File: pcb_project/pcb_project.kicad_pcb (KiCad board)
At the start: 6 copper layers, 246 parts, among them IC1 TPS54325PWPR, IC2 TPS54294PWPR, IC3 IS61WV204816BLL-10TLI, IC4 IS61WV204816BLL-10TLI, J1 USB1130-15-A_REVA, J10 M20-9990246, J11 M20-9990246, J12 M20-9990246, J13 Conn_01x10_Pin, J2 FTSH-107-01-F-DV-K, J3 Conn_ST_STDC14, J4 DE15_Socket_HighDensity_Mount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, J5 USB_B_Micro, J6 MEM2052-00-195-00-A, J8 M20-9990246, J9 M20-9990246, Q1 BC857BS, Q2 BC847BPN, SW2 SW_SPDT, SW3 SW_SPST, SW4 SW_SPST, U1 XC7A100T-FTG256, U10 TPD1E1B04DPYT, U11 TPD1E1B04DPYT, U12 TPD1E1B04DPYT, U13 TPD1E1B04DPYT, U2 STM32U595VJTx, U3 TPS2041B, U4 D3V3XA4B10LP, U5 TPD1E1B04DPYT, U6 TPD1E1B04DPYT, U7 MAX7221xWG, U8 COM-11405, U9 MT25QL128ABA1ESE-0SIT, Y1 48MHz, Y2 XLH736025.175000I

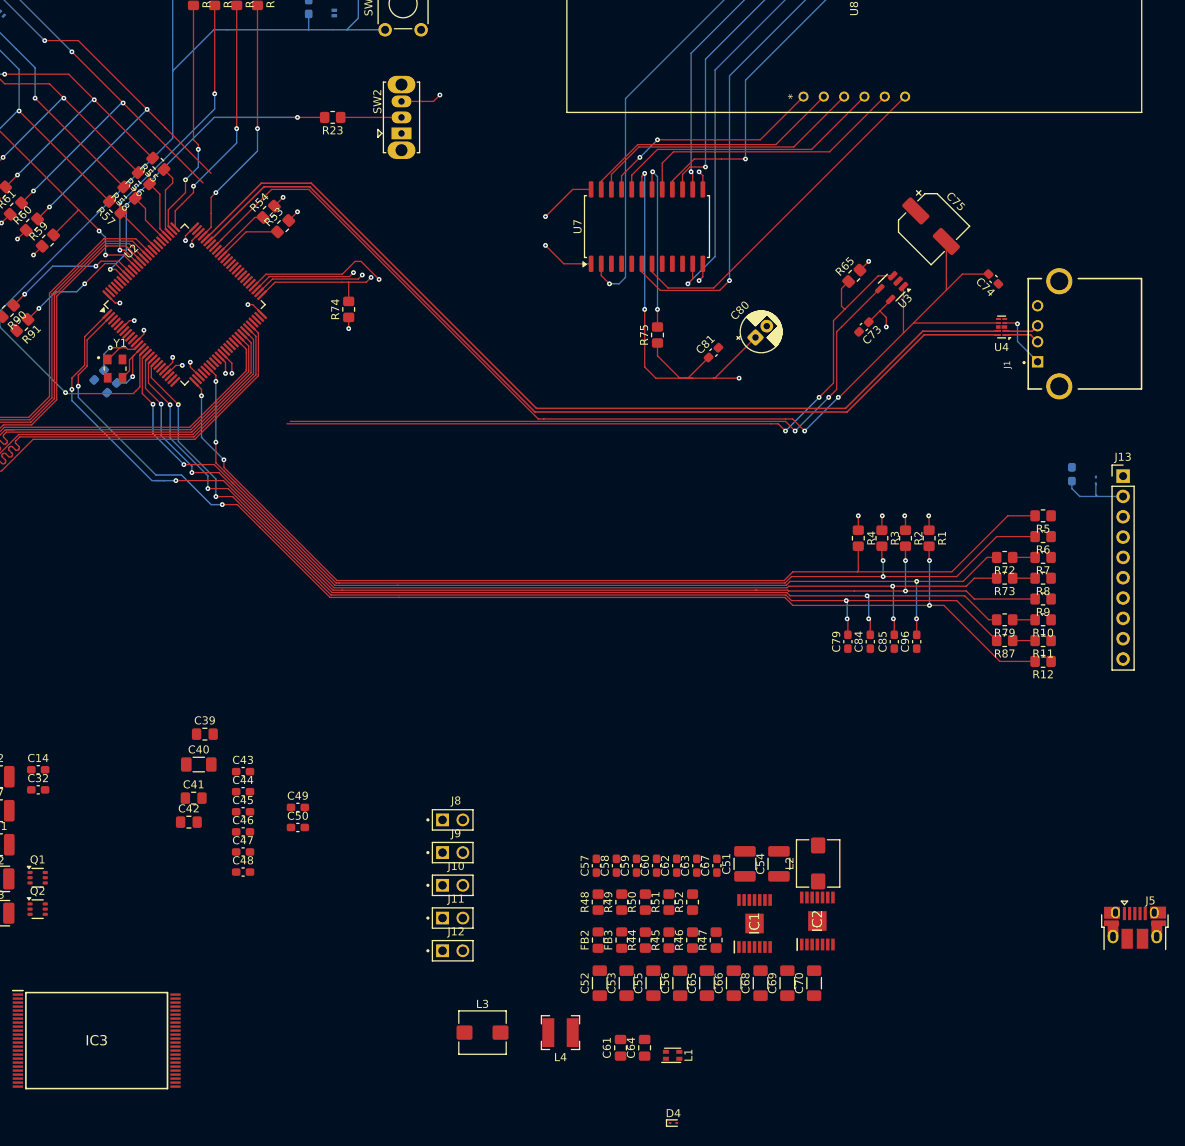
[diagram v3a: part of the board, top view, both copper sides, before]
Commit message: Power supply layout
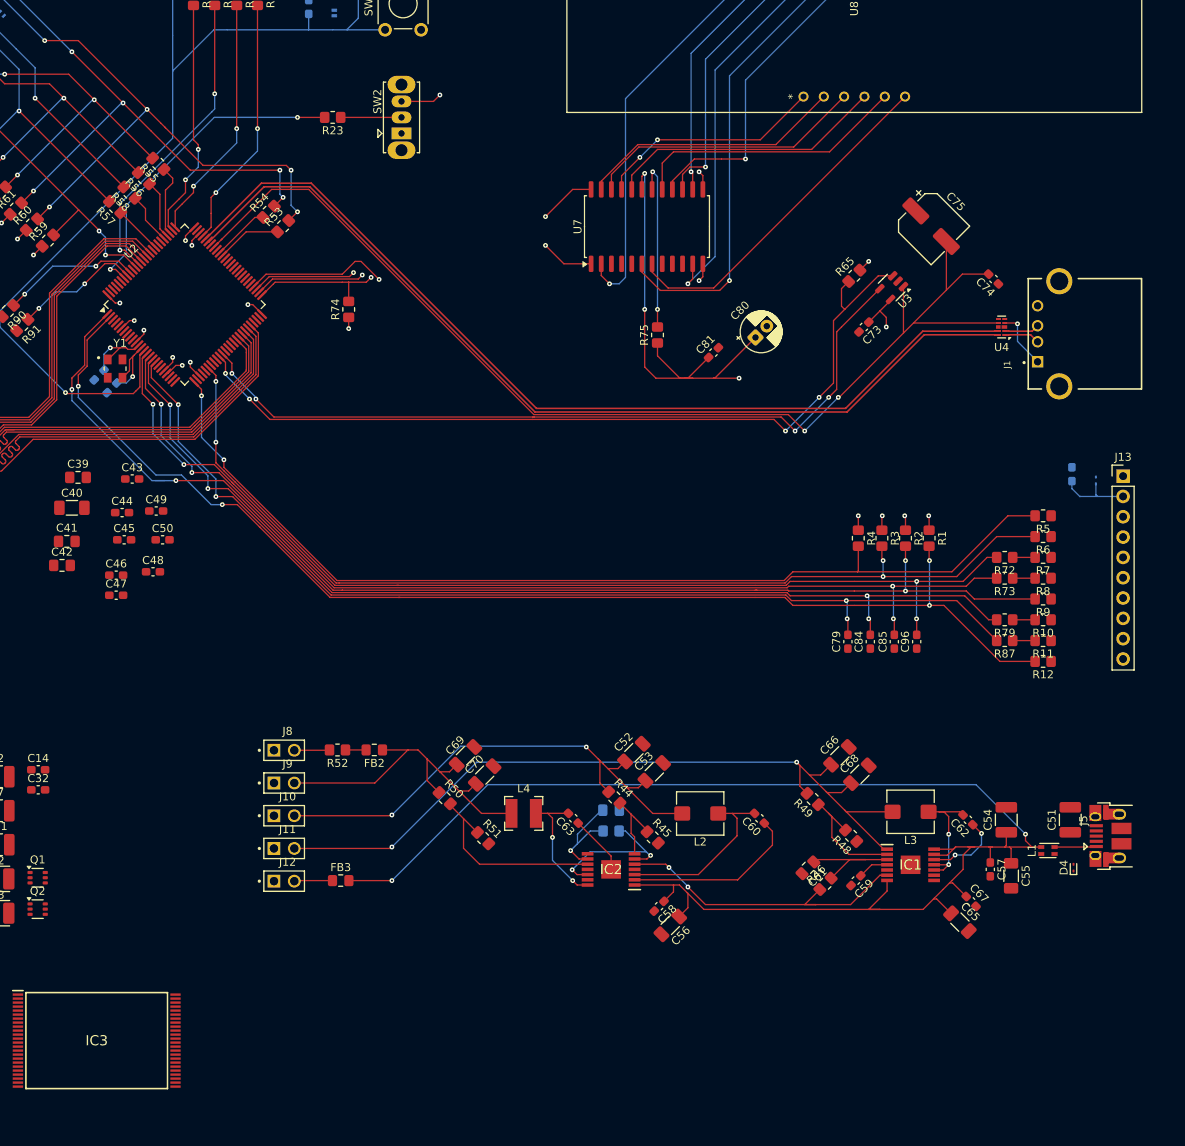
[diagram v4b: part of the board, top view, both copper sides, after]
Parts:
- C64, R47: moved to B.Cu
- moved L3 60.2 mm to (233.2, 133.4), turned to 180 degrees
- moved D4 59.3 mm to (253.6, 140.4), turned to 90 degrees
- moved L1 53.4 mm to (250.4, 138.2), turned to -90 degrees
- moved C69 49.3 mm to (177.6, 126.4), turned to 45 degrees
- moved C57 49.2 mm to (243.2, 140.6), turned to -90 degrees
- moved C70 48.7 mm to (180.0, 128.8), turned to 45 degrees
- moved R52 48.3 mm to (161.6, 125.7), turned to 180 degrees
- moved C55 46.7 mm to (245.8, 141.4), turned to -90 degrees
- moved C49 41.1 mm to (138.9, 95.8)
- moved C51 41.0 mm to (253.2, 134.4)
- moved C50 39.7 mm to (139.7, 99.4)
- moved C48 39.2 mm to (138.5, 103.4)
- moved C43 39.1 mm to (135.9, 91.8)
- moved C44 38.0 mm to (134.7, 96.0)
- moved C45 37.1 mm to (134.9, 99.4)
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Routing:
- net Net-(IC1-EN): track 0.00 -> 182.8 mm, vias 0 -> 2
- net Net-(IC1-VO): track 0.00 -> 100.1 mm, vias 0 -> 2
- net Net-(C52-Pad1): track 0.00 -> 65.8 mm, vias 0 -> 2
- net Net-(C69-Pad1): track 0.00 -> 45.0 mm
- net Net-(IC1-PG): track 0.00 -> 39.3 mm, vias 0 -> 2
- net Net-(IC2-VFB2): track 0.00 -> 25.0 mm
- net Net-(IC2-SW1): track 0.00 -> 22.4 mm
- net Net-(IC2-VBST1): track 0.00 -> 22.2 mm
- net Net-(IC2-EN2): track 0.00 -> 19.8 mm, vias 0 -> 2
- net Net-(IC2-SW2): track 0.00 -> 15.9 mm, vias 0 -> 2
- net Net-(IC1-SW1): track 0.00 -> 15.9 mm, vias 0 -> 2
- net Net-(IC1-VFB): track 0.00 -> 15.6 mm
- net Net-(J6-DAT0): track 64.1 -> 79.4 mm, vias 5 -> 6
- net Net-(IC1-VREG5): track 0.00 -> 14.5 mm
- net Net-(IC2-VREG5): track 0.00 -> 13.2 mm, vias 0 -> 1
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
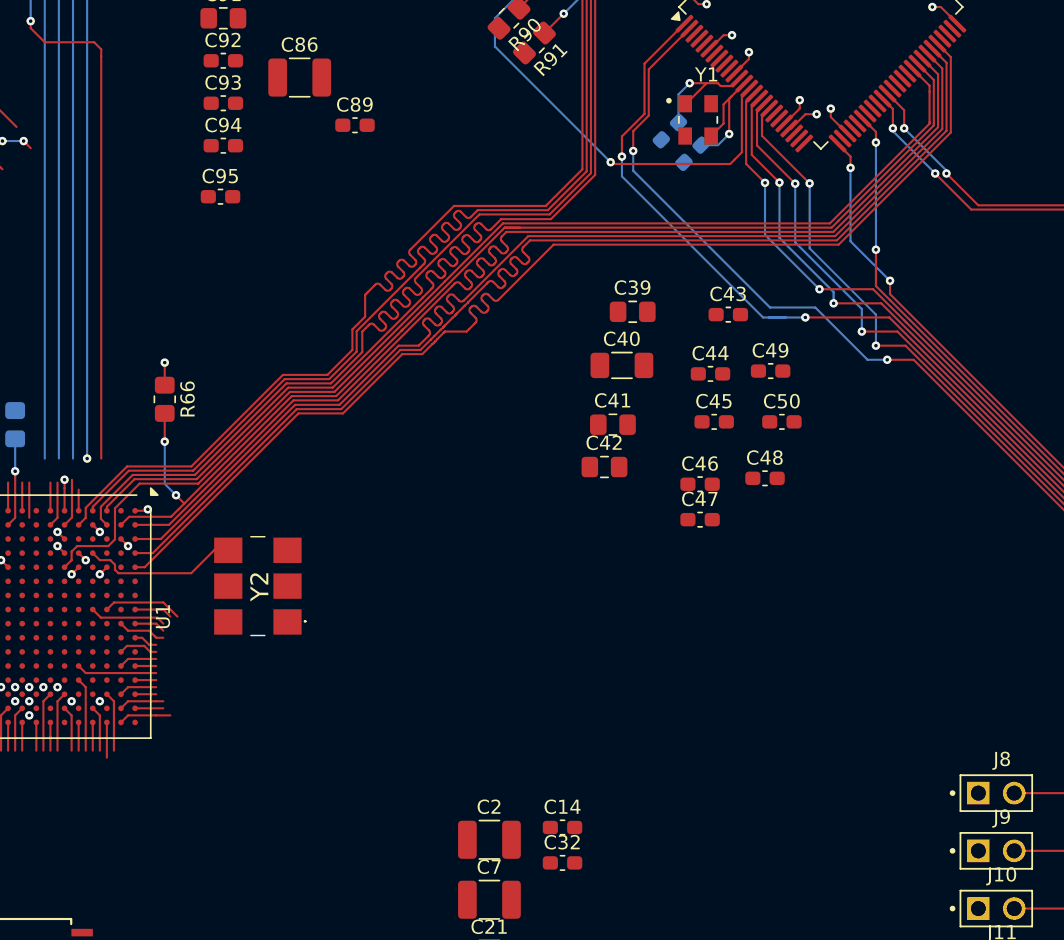
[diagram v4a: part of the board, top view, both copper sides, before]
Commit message: More length matching OSPI
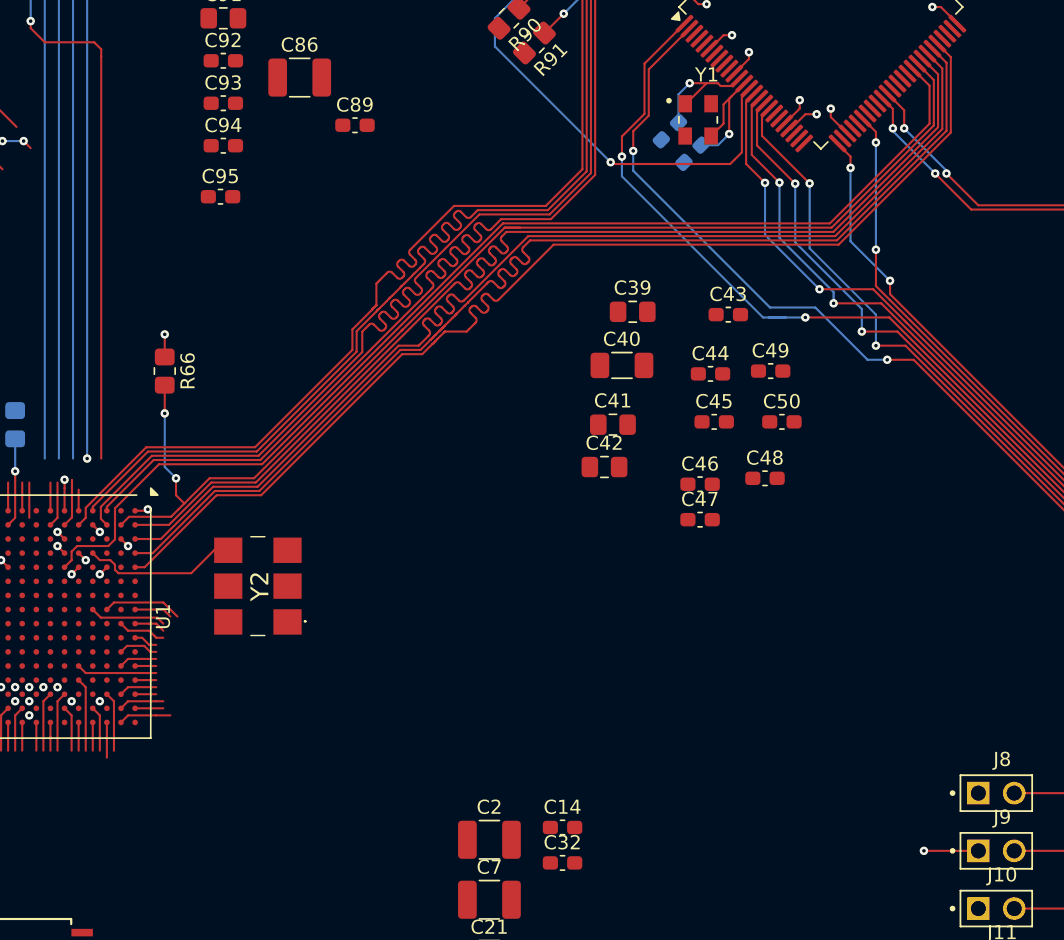
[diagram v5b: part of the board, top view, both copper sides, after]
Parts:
- moved R66 2.00 mm to (96.0, 95.8)
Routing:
- net +3V3: track 81.3 -> 85.2 mm, vias 28 -> 29
- net /FPGA/OSPI CS: track 82.4 -> 84.4 mm
- net /FPGA/OSPI 4: track 82.0 -> 80.4 mm

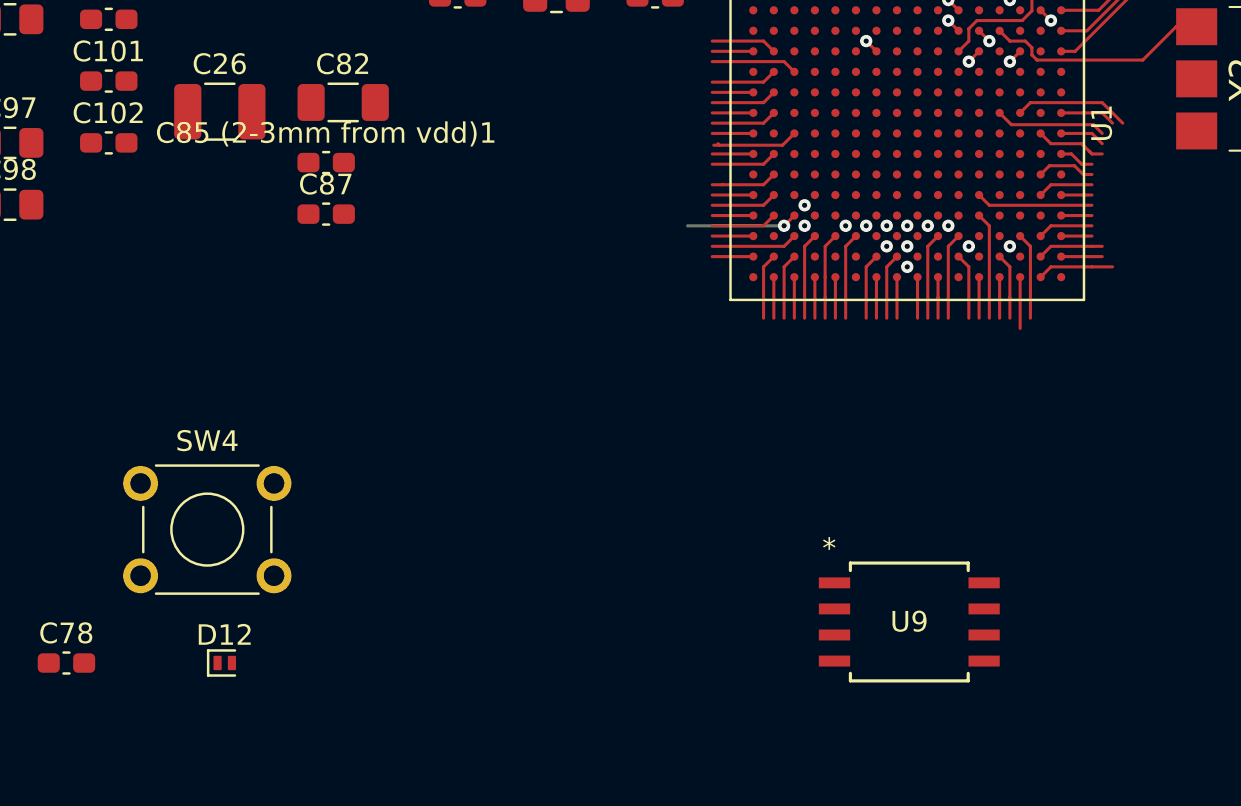
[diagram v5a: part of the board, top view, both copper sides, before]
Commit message: More fpga outwires
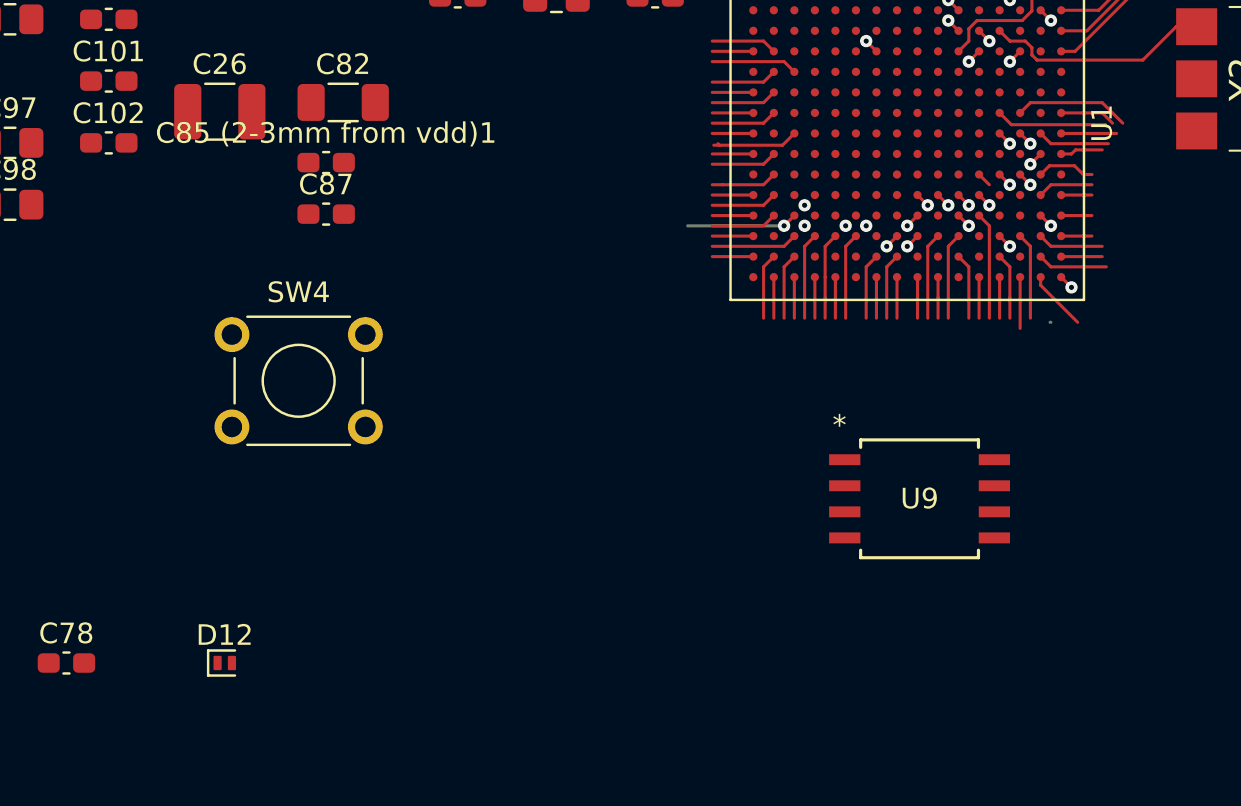
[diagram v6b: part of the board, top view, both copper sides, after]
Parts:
- moved SW4 8.51 mm to (53.5, 123.5)
- moved U9 6.02 mm to (87.0, 131.5)
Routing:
- net /FPGA/A_Bank14&15/WE: track 0.00 -> 9.17 mm, vias 0 -> 1
- net Net-(IC3-I/O8): track 0.00 -> 8.55 mm, vias 0 -> 1
- net Net-(IC3-I/O3): track 0.00 -> 8.26 mm, vias 0 -> 1
- net Net-(IC3-I/O4): track 0.00 -> 7.35 mm, vias 0 -> 1
- net Net-(IC3-A11): track 0.00 -> 6.13 mm, vias 0 -> 1
- net /FPGA/A_Bank14&15/LB: track 0.00 -> 5.80 mm, vias 0 -> 1
- net Net-(IC3-A1): track 0.00 -> 4.88 mm, vias 0 -> 1
- net Net-(IC3-A6): track 0.00 -> 4.85 mm, vias 0 -> 1
- net Net-(U1A-IO_L1N_T0_D01_DIN_14): track 0.00 -> 4.63 mm, vias 0 -> 1
- net /FPGA/A_Bank14&15/A20: track 0.00 -> 4.60 mm, vias 0 -> 1
- net Net-(IC3-I/O15): track 0.00 -> 4.60 mm, vias 0 -> 1
- net Net-(IC3-I/O0): track 5.71 -> 8.32 mm, vias 0 -> 1
- net +3V3: track 85.2 -> 86.6 mm, vias 29 -> 31
- net Net-(IC3-A19): track 3.71 -> 2.95 mm
- net Net-(IC3-I/O9): track 0.00 -> 0.71 mm, vias 0 -> 1
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
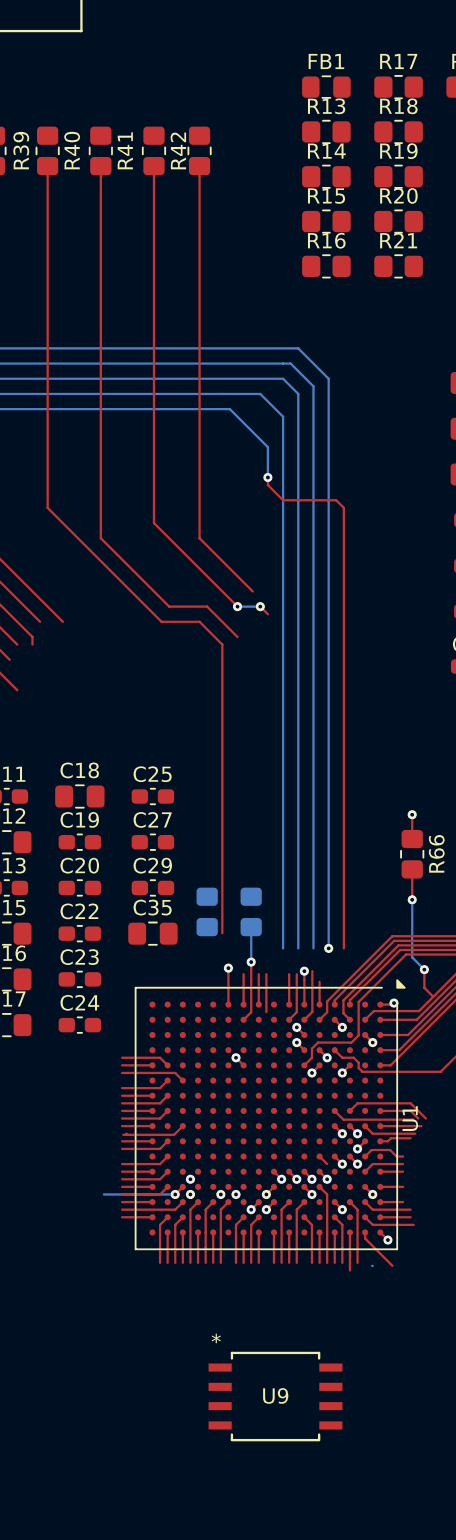
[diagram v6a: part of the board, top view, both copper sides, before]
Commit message: More FPGA ballout
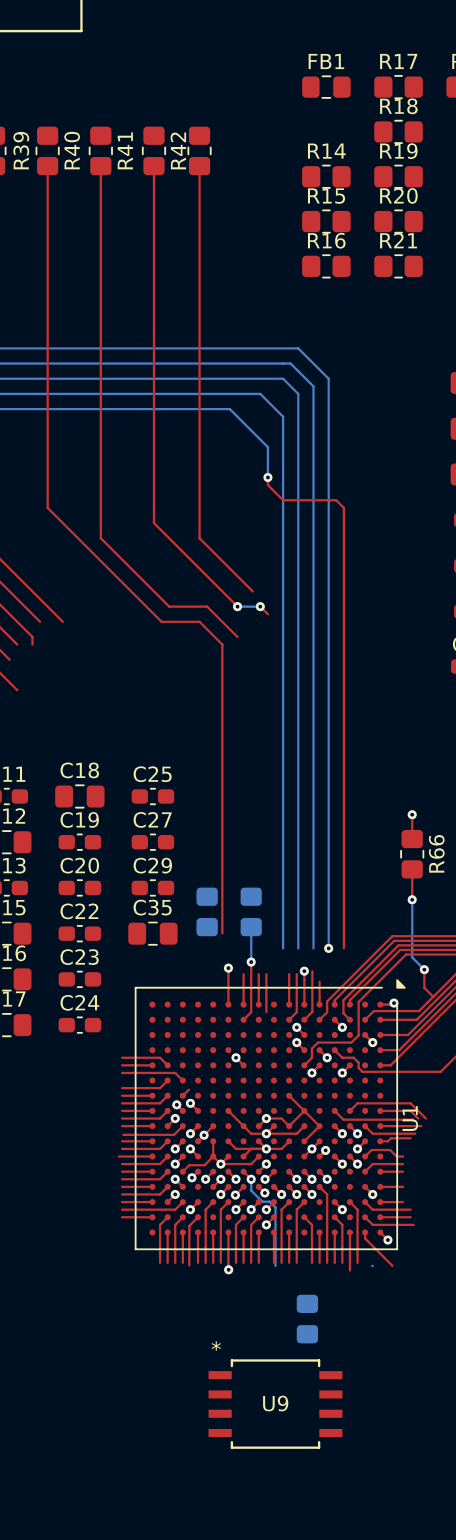
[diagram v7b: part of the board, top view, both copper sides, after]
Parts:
- R13: moved to B.Cu
- moved R13 78.2 mm to (89.1, 126.4), turned to -90 degrees
- moved U9 0.50 mm to (87.0, 132.0)
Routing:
- net GND: track 5.53 -> 26.7 mm, vias 4 -> 9
- net +3V3: track 86.6 -> 96.1 mm, vias 31 -> 37
- net Net-(IC4-LB#): track 0.00 -> 8.44 mm, vias 0 -> 1
- net Net-(U1A-IO_L6P_T0_FCS_B_14): track 0.00 -> 8.00 mm, vias 0 -> 1
- net +1V0: track 0.00 -> 7.95 mm, vias 0 -> 2
- net Net-(IC4-I/O15): track 0.00 -> 7.36 mm, vias 0 -> 1
- net Net-(IC3-I/O2): track 0.71 -> 8.06 mm, vias 0 -> 1
- net +1V8: track 0.00 -> 6.83 mm, vias 0 -> 1
- net Net-(IC4-UB#): track 0.00 -> 6.54 mm, vias 0 -> 1
- net Net-(IC4-WE#): track 0.00 -> 6.47 mm, vias 0 -> 1
- net Net-(IC4-I/O0): track 0.00 -> 5.75 mm, vias 0 -> 1
- net Net-(U1C-TDO_0): track 0.00 -> 5.71 mm, vias 0 -> 1
- net Net-(IC4-I/O1): track 0.00 -> 5.64 mm, vias 0 -> 1
- net Net-(IC4-A12): track 0.00 -> 5.49 mm, vias 0 -> 1
- net Net-(U1A-IO_L1P_T0_D00_MOSI_14): track 0.00 -> 5.47 mm, vias 0 -> 1
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
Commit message: Set PCB size
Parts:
- C29: moved to B.Cu
- moved C48 158.8 mm to (296.5, 87.7)
- moved C47 158.8 mm to (291.9, 90.6)
- moved C49 158.8 mm to (296.9, 80.1)
- moved C50 158.8 mm to (297.7, 83.7)
- moved C42 158.7 mm to (285.2, 88.1), turned to 90 degrees
- moved C41 155.0 mm to (282.2, 87.5), turned to 90 degrees
- moved C46 154.2 mm to (286.5, 81.3), turned to 90 degrees
- moved C40 149.9 mm to (278.1, 86.9), turned to 90 degrees
- moved C45 148.3 mm to (282.1, 80.3), turned to 90 degrees
- moved C44 144.8 mm to (278.6, 80.6), turned to 90 degrees
- moved C39 141.1 mm to (269.8, 79.6)
- moved C43 134.6 mm to (270.3, 83.7)
- moved J2 81.4 mm to (63.2, 78.6), turned to 90 degrees
- moved C88 67.5 mm to (36.0, 44.0)
- moved C90 67.5 mm to (36.0, 47.0)
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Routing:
- net /VGA/R0: track 103.8 -> 4.24 mm, vias 3 -> 1
- net /VGA/R2: track 98.1 -> 2.12 mm, vias 2 -> 1
- net /VGA/R1: track 98.9 -> 5.33 mm, vias 2 -> 1
- net /VGA/R3: track 99.4 -> 6.04 mm, vias 1 -> 0
- net /VGA/R4: track 96.4 -> 4.33 mm, vias 2 -> 1
- net /FPGA/OSPI 3: track 80.4 -> 38.8 mm
- net /FPGA/OSPI CS: track 84.4 -> 43.2 mm, vias 2 -> 0
- net /FPGA/OSPI 2: track 80.8 -> 40.9 mm
- net /FPGA/OSPI 1: track 79.7 -> 40.1 mm
- net /FPGA/OSPI 7: track 79.3 -> 40.8 mm
- net /FPGA/OSPI 0: track 80.1 -> 41.8 mm
- net /VGA/G0: track 38.2 -> 0.00 mm
- net /FPGA/OSPI 6: track 80.6 -> 43.3 mm
- net /FPGA/OSPI 5: track 80.5 -> 43.7 mm
- net /VGA/B2: track 36.2 -> 0.00 mm
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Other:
- board outline added: 207.7 x 108.2 mm
